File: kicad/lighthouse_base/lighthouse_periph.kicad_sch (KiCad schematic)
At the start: 3 parts, among them J3 Conn_01x12, J4 Conn_01x12, J5 Conn_01x06

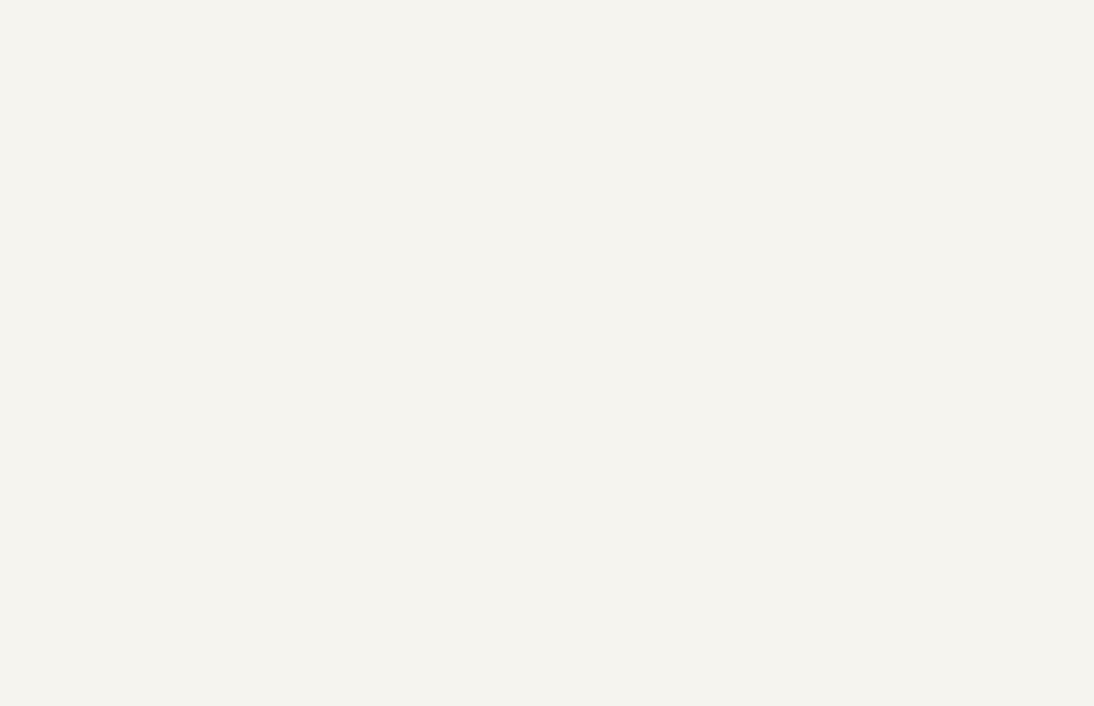
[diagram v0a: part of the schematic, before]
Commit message: added FPPlayer and BC805M BLE Module
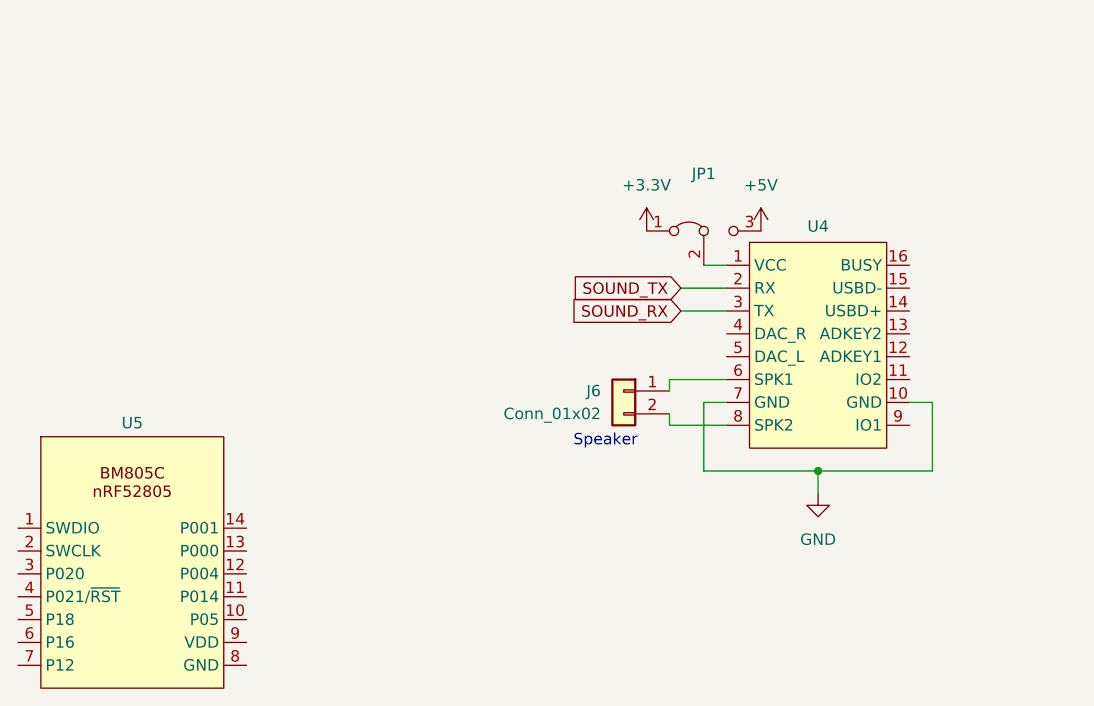
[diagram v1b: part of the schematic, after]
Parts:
- added J6: Conn_01x02, symbol Connector_Generic:Conn_01x02
- added JP1: Jumper_3_Bridged12, symbol Jumper:Jumper_3_Bridged12
- added U4: ~, lighthouse:DFPlayer_Mini-TF-16P, symbol lighthouse1:DFPlayer_Mini
- added U5: ~, lighthouse:BC805M, symbol lighthouse1:BC805M_nRF52805
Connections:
- net +3.3V: now also JP1.1 (A)
- net +5V: now also JP1.3 (B)
- net GND: now also U4.10 (GND), U4.7 (GND)
- new net: JP1.2 (C), U4.1 (VCC)
- new net: J6.1 (Pin_1), U4.6 (SPK1)
- new net: J6.2 (Pin_2), U4.8 (SPK2)
- new net SOUND_RX: U4.3 (TX)
- new net SOUND_TX: U4.2 (RX)
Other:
- note added: "Speaker"

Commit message: schema v1 done
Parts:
- added J7: Conn_01x05, symbol Connector_Generic:Conn_01x05
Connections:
- net +3.3V: now also U5.9 (VDD), J7.1 (Pin_1)
- net GND: now also U5.8 (GND), J7.2 (Pin_2)
- net at U5.1 (SWDIO): now also J7.3 (Pin_3)
- net BLE_TX: now reaches U5.10 (P05)
- net BLE_RX: now reaches U5.11 (P014)
- net at U5.2 (SWCLK): now also J7.4 (Pin_4)
- net at U5.4 (P021/~{RST}): now also J7.5 (Pin_5)
- net WHITE_PWM renamed WHITE_PWM1
- net WHITE_PWM1: no longer J4.9 (Pin_9)
- new net WHITE_PWM2: J4.9 (Pin_9)
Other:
- moved on the sheet: J3, J4, J5, U5

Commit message: schematics done
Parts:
- J4: renamed from J3; footprint (none) -> Connector_Molex:Molex_Picoflex_90325-0012_2x06_P1.27mm_Vertical
- J5: renamed from J4; footprint (none) -> Connector_Molex:Molex_Picoflex_90325-0012_2x06_P1.27mm_Vertical
- J6: renamed from J5; footprint (none) -> Connector_Molex:Molex_Picoflex_90325-0006_2x03_P1.27mm_Vertical
- J7: renamed from J6; footprint (none) -> Connector_PinHeader_2.54mm:PinHeader_1x02_P2.54mm_Vertical
- J8: renamed from J7; footprint (none) -> Connector_PinHeader_1.27mm:PinHeader_1x05_P1.27mm_Vertical
- JP1: footprint (none) -> Jumper:SolderJumper-3_P1.3mm_Bridged2Bar12_RoundedPad1.0x1.5mm
- renumbered U4 to U8, U5 to U9
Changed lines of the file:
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@@
 		(dnp no)
 		(fields_autoplaced yes)
-		(property "Reference" "J5"
+		(property "Reference" "J6"
 			(at 264.16 124.4599 0)
 			(effects
@@
 			)
 		)
-		(property "Footprint" ""
+		(property "Footprint" "Connector_Molex:Molex_Picoflex_90325-0006_2x03_P1.27mm_Vertical"
 			(at 261.62 124.46 0)
 			(effects
@@
 			(project "lighthouse_base"
 				(path "/e329df4a-6588-455a-9936-c9675a4aa830/0766630d-8ec2-4c83-94b4-820a1d6c29c4"
-					(reference "J5")
+					(reference "J6")
 					(unit 1)
 				)
@@
 		(dnp no)
 		(fields_autoplaced yes)
-		(property "Reference" "#PWR07"
+		(property "Reference" "#PWR026"
 			(at 254 139.7 0)
 			(effects
@@
 			(project "lighthouse_base"
 				(path "/e329df4a-6588-455a-9936-c9675a4aa830/0766630d-8ec2-4c83-94b4-820a1d6c29c4"
-					(reference "#PWR07")
+					(reference "#PWR026")
 					(unit 1)
 				)
@@
 		(dnp no)
 		(fields_autoplaced yes)
-		(property "Reference" "J3"
+		(property "Reference" "J4"
 			(at 264.16 50.7999 0)
 			(effects
@@
 			)
 		)
-		(property "Footprint" ""
+		(property "Footprint" "Connector_Molex:Molex_Picoflex_90325-0012_2x06_P1.27mm_Vertical"
 			(at 261.62 50.8 0)
 			(effects
@@
 			(project "lighthouse_base"
 				(path "/e329df4a-6588-455a-9936-c9675a4aa830/0766630d-8ec2-4c83-94b4-820a1d6c29c4"
-					(reference "J3")
+					(reference "J4")
 					(unit 1)
 				)
@@
 			)
 		)
-		(property "Footprint" ""
+		(property "Footprint" "Jumper:SolderJumper-3_P1.3mm_Bridged2Bar12_RoundedPad1.0x1.5mm"
 			(at 173.99 124.46 0)
 			(effects
@@
 		(on_board yes)
 		(dnp no)
-		(property "Reference" "#PWR05"
+		(property "Reference" "#PWR022"
 			(at 246.38 36.83 0)
 			(effects
@@
 			(project "lighthouse_base"
 				(path "/e329df4a-6588-455a-9936-c9675a4aa830/0766630d-8ec2-4c83-94b4-820a1d6c29c4"
-					(reference "#PWR05")
+					(reference "#PWR022")
 					(unit 1)
 				)
@@
 		(on_board yes)
 		(dnp no)
-		(property "Reference" "U4"
+		(property "Reference" "U8"
 			(at 186.69 123.952 0)
 			(effects
@@
 			(project ""
 				(path "/e329df4a-6588-455a-9936-c9675a4aa830/0766630d-8ec2-4c83-94b4-820a1d6c29c4"
-					(reference "U4")
+					(reference "U8")
 					(unit 1)
 				)
@@
 		(on_board yes)
 		(dnp no)
-		(property "Reference" "#PWR015"
+		(property "Reference" "#PWR025"
 			(at 180.34 128.27 0)
 			(effects
@@
 			(project "lighthouse_base"
 				(path "/e329df4a-6588-455a-9936-c9675a4aa830/0766630d-8ec2-4c83-94b4-820a1d6c29c4"
-					(reference "#PWR015")
+					(reference "#PWR025")
 					(unit 1)
 				)
@@
 		(dnp no)
 		(fields_autoplaced yes)
-		(property "Reference" "J4"
+		(property "Reference" "J5"
 			(at 264.16 88.8999 0)
 			(effects
@@
 			)
 		)
-		(property "Footprint" ""
+		(property "Footprint" "Connector_Molex:Molex_Picoflex_90325-0012_2x06_P1.27mm_Vertical"
 			(at 261.62 88.9 0)
 			(effects
@@
 			(project "lighthouse_base"
 				(path "/e329df4a-6588-455a-9936-c9675a4aa830/0766630d-8ec2-4c83-94b4-820a1d6c29c4"
-					(reference "J4")
+					(reference "J5")
 					(unit 1)
 				)
@@
 		(on_board yes)
 		(dnp no)
-		(property "Reference" "J7"
+		(property "Reference" "J8"
 			(at 73.66 156.2099 0)
 			(effects
@@
 			)
 		)
-		(property "Footprint" ""
+		(property "Footprint" "Connector_PinHeader_1.27mm:PinHeader_1x05_P1.27mm_Vertical"
 			(at 76.2 157.48 0)
 			(effects
@@
 			(project ""
 				(path "/e329df4a-6588-455a-9936-c9675a4aa830/0766630d-8ec2-4c83-94b4-820a1d6c29c4"
-					(reference "J7")
+					(reference "J8")
 					(unit 1)
 				)
@@
 		(dnp no)
 		(fields_autoplaced yes)
-		(property "Reference" "#PWR016"
+		(property "Reference" "#PWR024"
 			(at 167.64 128.27 0)
 			(effects
@@
 			(project "lighthouse_base"
 				(path "/e329df4a-6588-455a-9936-c9675a4aa830/0766630d-8ec2-4c83-94b4-820a1d6c29c4"
-					(reference "#PWR016")
+					(reference "#PWR024")
 					(unit 1)
 				)
@@
 		(dnp no)
 		(fields_autoplaced yes)
-		(property "Reference" "#PWR04"
+		(property "Reference" "#PWR021"
 			(at 241.3 36.83 0)
 			(effects
@@
 			(project "lighthouse_base"
 				(path "/e329df4a-6588-455a-9936-c9675a4aa830/0766630d-8ec2-4c83-94b4-820a1d6c29c4"
-					(reference "#PWR04")
+					(reference "#PWR021")
 					(unit 1)
 				)
@@
 		(on_board yes)
 		(dnp no)
-		(property "Reference" "J6"
+		(property "Reference" "J7"
 			(at 162.56 142.2399 0)
 			(effects
@@
 			)
 		)
-		(property "Footprint" ""
+		(property "Footprint" "Connector_PinHeader_2.54mm:PinHeader_1x02_P2.54mm_Vertical"
 			(at 165.1 142.24 0)
 			(effects
@@
 			(project ""
 				(path "/e329df4a-6588-455a-9936-c9675a4aa830/0766630d-8ec2-4c83-94b4-820a1d6c29c4"
-					(reference "J6")
+					(reference "J7")
 					(unit 1)
 				)
@@
 		(dnp no)
 		(fields_autoplaced yes)
-		(property "Reference" "#PWR018"
+		(property "Reference" "#PWR030"
 			(at 83.82 171.45 0)
 			(effects
@@
 			(project "lighthouse_base"
 				(path "/e329df4a-6588-455a-9936-c9675a4aa830/0766630d-8ec2-4c83-94b4-820a1d6c29c4"
-					(reference "#PWR018")
+					(reference "#PWR030")
 					(unit 1)
 				)
@@
 		(on_board yes)
 		(dnp no)
-		(property "Reference" "U5"
+		(property "Reference" "U9"
 			(at 109.22 145.796 0)
 			(effects
@@
 			(project ""
 				(path "/e329df4a-6588-455a-9936-c9675a4aa830/0766630d-8ec2-4c83-94b4-820a1d6c29c4"
-					(reference "U5")
+					(reference "U9")
 					(unit 1)
 				)
@@
 		(dnp no)
 		(fields_autoplaced yes)
-		(property "Reference" "#PWR014"
+		(property "Reference" "#PWR027"
 			(at 83.82 153.67 0)
 			(effects
@@
 			(project "lighthouse_base"
 				(path "/e329df4a-6588-455a-9936-c9675a4aa830/0766630d-8ec2-4c83-94b4-820a1d6c29c4"
-					(reference "#PWR014")
+					(reference "#PWR027")
 					(unit 1)
 				)
@@
 		(dnp no)
 		(fields_autoplaced yes)
-		(property "Reference" "#PWR06"
+		(property "Reference" "#PWR023"
 			(at 251.46 36.83 0)
 			(effects
@@
 			(project "lighthouse_base"
 				(path "/e329df4a-6588-455a-9936-c9675a4aa830/0766630d-8ec2-4c83-94b4-820a1d6c29c4"
-					(reference "#PWR06")
+					(reference "#PWR023")
 					(unit 1)
 				)
@@
 		(dnp no)
 		(fields_autoplaced yes)
-		(property "Reference" "#PWR019"
+		(property "Reference" "#PWR029"
 			(at 124.46 158.75 0)
 			(effects
@@
 			(project "lighthouse_base"
 				(path "/e329df4a-6588-455a-9936-c9675a4aa830/0766630d-8ec2-4c83-94b4-820a1d6c29c4"
-					(reference "#PWR019")
+					(reference "#PWR029")
 					(unit 1)
 				)
@@
 		(dnp no)
 		(fields_autoplaced yes)
-		(property "Reference" "#PWR017"
+		(property "Reference" "#PWR028"
 			(at 186.69 160.02 0)
 			(effects
@@
 			(project "lighthouse_base"
 				(path "/e329df4a-6588-455a-9936-c9675a4aa830/0766630d-8ec2-4c83-94b4-820a1d6c29c4"
-					(reference "#PWR017")
+					(reference "#PWR028")
 					(unit 1)
 				)
@@
 		(dnp no)
 		(fields_autoplaced yes)
-		(property "Reference" "#PWR020"
+		(property "Reference" "#PWR031"
 			(at 124.46 181.61 0)
 			(effects
@@
 			(project "lighthouse_base"
 				(path "/e329df4a-6588-455a-9936-c9675a4aa830/0766630d-8ec2-4c83-94b4-820a1d6c29c4"
-					(reference "#PWR020")
-					(unit 1)
-				)
+					(reference "#PWR031")
+					(unit 1)
+				)

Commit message: started with pcb lighthouse_base
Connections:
- no-connect marks 0 -> 22
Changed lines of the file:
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@@
 		(color 0 0 0 0)
+	)
+	(no_connect
+		(at 121.92 162.56)
+	)
+	(no_connect
+		(at 196.85 133.35)
+	)
+	(no_connect
+		(at 121.92 160.02)
+	)
+	(no_connect
+		(at 256.54 66.04)
+	)
+	(no_connect
+		(at 176.53 135.89)
+	)
+	(no_connect
+		(at 196.85 138.43)
+	)
+	(no_connect
+		(at 256.54 99.06)
+	)
+	(no_connect
+		(at 176.53 138.43)
+	)
+	(no_connect
+		(at 256.54 60.96)
+	)
+	(no_connect
+		(at 196.85 135.89)
+	)
+	(no_connect
+		(at 96.52 170.18)
+	)
+	(no_connect
+		(at 96.52 172.72)
+	)
+	(no_connect
+		(at 196.85 128.27)
+	)
+	(no_connect
+		(at 256.54 63.5)
+	)
+	(no_connect
+		(at 121.92 157.48)
+	)
+	(no_connect
+		(at 196.85 130.81)
+	)
+	(no_connect
+		(at 96.52 167.64)
+	)
+	(no_connect
+		(at 196.85 140.97)
+	)
+	(no_connect
+		(at 256.54 101.6)
+	)
+	(no_connect
+		(at 196.85 146.05)
+	)
+	(no_connect
+		(at 96.52 162.56)
+	)
+	(no_connect
+		(at 256.54 104.14)
 	)
 	(wire

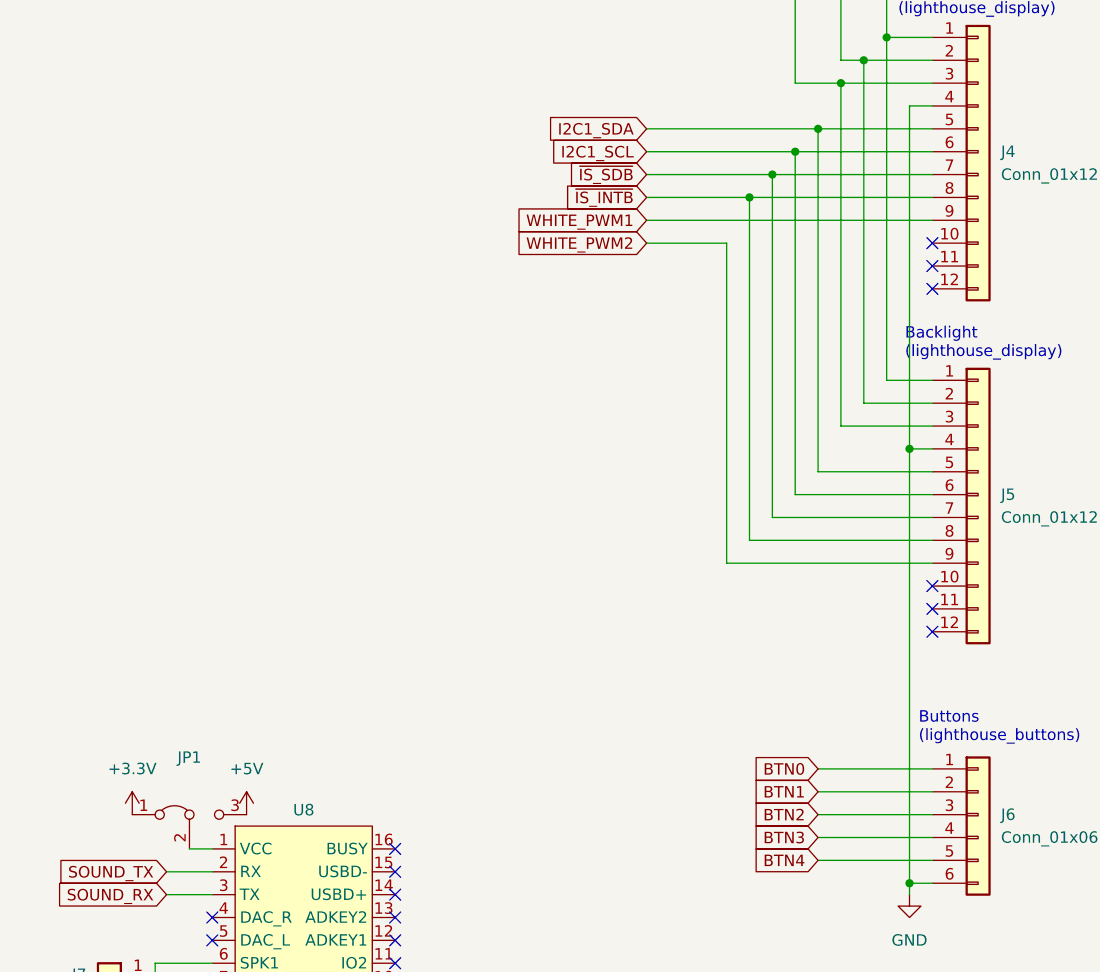
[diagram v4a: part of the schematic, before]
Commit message: rev1: added 32 kHz XTAL, interrupt signals for VBUS + +5V, ... many more
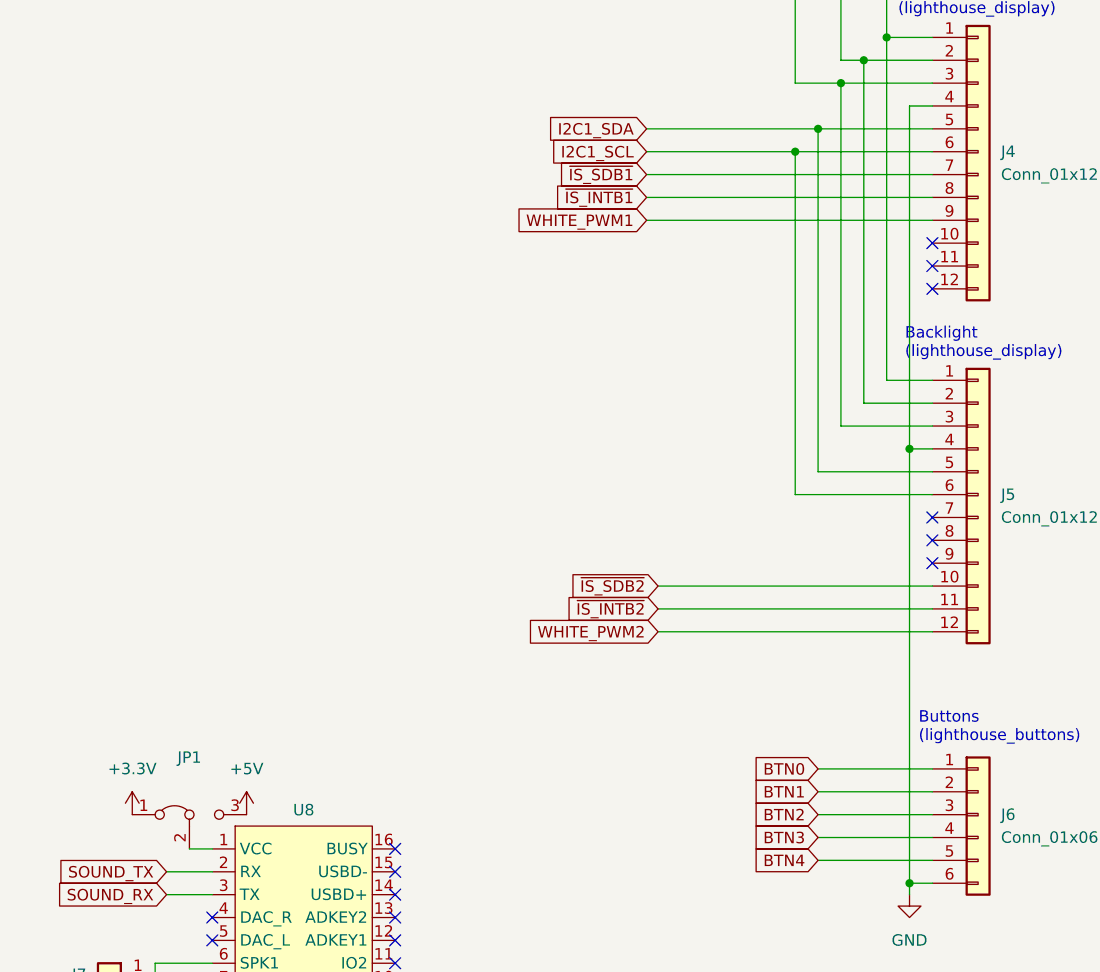
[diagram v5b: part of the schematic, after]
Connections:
- net WHITE_PWM2: now also J5.12 (Pin_12); no longer J5.9 (Pin_9)
- net ~{IS_SDB2}: now reaches J5.10 (Pin_10)
- net ~{IS_INTB2}: now reaches J5.11 (Pin_11)
- net ~{IS_INTB}: no longer names the net of J5.8 (Pin_8)
- net ~{IS_INTB}: no longer J4.8 (Pin_8)
- net ~{IS_SDB}: no longer names the net of J5.7 (Pin_7)
- net ~{IS_SDB}: no longer J4.7 (Pin_7)
- new net ~{IS_INTB1}: J4.8 (Pin_8)
- new net ~{IS_SDB1}: J4.7 (Pin_7)

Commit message: ordererd lighthouse display
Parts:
- J4, J5, J6, J7, J8, U8, U9: now left out of the parts list
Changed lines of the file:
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@@
 		(unit 1)
 		(exclude_from_sim no)
-		(in_bom yes)
+		(in_bom no)
 		(on_board yes)
 		(dnp no)
@@
 		(unit 1)
 		(exclude_from_sim no)
-		(in_bom yes)
+		(in_bom no)
 		(on_board yes)
 		(dnp no)
@@
 		(unit 1)
 		(exclude_from_sim no)
-		(in_bom yes)
+		(in_bom no)
 		(on_board yes)
 		(dnp no)
@@
 		(unit 1)
 		(exclude_from_sim no)
-		(in_bom yes)
+		(in_bom no)
 		(on_board yes)
 		(dnp no)
@@
 		(unit 1)
 		(exclude_from_sim no)
-		(in_bom yes)
+		(in_bom no)
 		(on_board yes)
 		(dnp no)
@@
 		(unit 1)
 		(exclude_from_sim no)
-		(in_bom yes)
+		(in_bom no)
 		(on_board yes)
 		(dnp no)
@@
 		(unit 1)
 		(exclude_from_sim no)
-		(in_bom yes)
-		(on_board yes)
-		(dnp no)
+		(in_bom no)
+		(on_board yes)
+		(dnp no)
